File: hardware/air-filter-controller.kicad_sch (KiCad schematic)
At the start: 42 parts, among them J1 TYPE-C-31-M-12, J2 Barrel_Jack, J3 Conn_01x04, J4 Conn_01x03, SW1 SW_Push, SW2 SW_Push, U1 ESP32-S3-WROOM-1-N4, U2 BMP280, U3 MT2492

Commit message: First pass at schematic
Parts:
- removed J3: Conn_01x04, symbol Connector_Generic:Conn_01x04
- added D31, D32, D33, D34: SMAJ5.0A, Diode_SMD:D_SMA, symbol Device:D
- added J13, J14: Conn_01x02, symbol Connector_Generic:Conn_01x02
- added Q1: AO3400A, Package_TO_SOT_SMD:SOT-23, symbol Transistor_FET:AO3400A
- added R11: 100, Resistor_SMD:R_0402_1005Metric, symbol Device:R
- added R39, R40, R44, R45: 1k, Resistor_SMD:R_0402_1005Metric, symbol Device:R
- added R41: 680k, Resistor_SMD:R_0402_1005Metric, symbol Device:R
- added R42: 220k, Resistor_SMD:R_0402_1005Metric, symbol Device:R
- added R43: 10k, Resistor_SMD:R_0402_1005Metric, symbol Device:R
- added SW3, SW4: SW_Push, symbol Switch:SW_Push
- D1: LCSC (none) -> C22452; MPN (none) -> SS54
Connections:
- net USB_D+ is gone; now on net USB_DN: U1.14 (IO20)
- net USB_D- is gone; now on net USB_DP: U1.13 (IO19)
- net +12V: now also R41.1
- net CSB: now also U1.9 (IO16)
- net GND: now also D31.2 (A), D32.2 (A), D33.2 (A), D34.2 (A), J13.1 (Pin_1), J14.1 (Pin_1), Q1.2 (S), R42.2, SW3.2, SW4.2
- net SCK: now also U1.21 (IO13)
- net SDI: now also U1.22 (IO14)
- net SDO: now also U1.8 (IO15)
- net 12V_DIVIDED: now reaches U1.10 (IO17)
- net 12V_DIVIDED: now also R43.2
- net SW2: now reaches U1.11 (IO18)
- net SW2: now also D33.1 (K), R44.2
- net TACH4: now reaches U1.12 (IO8)
- net TACH5: now reaches U1.17 (IO9)
- net TACH6: now reaches U1.18 (IO10)
- net TACH7: now reaches U1.19 (IO11)
- net TACH8: now reaches U1.20 (IO12)
- net FAN_EN: now reaches U1.23 (IO21)
- net FAN_EN: now also R11.1
- net SW3: now reaches U1.31 (IO38)
- net SW3: now also D34.1 (K), R45.2
- net SW1: now reaches U1.38 (IO2)
- net SW1: now also D32.1 (K), R40.2
- net SW0: now reaches U1.39 (IO1)
- net SW0: now also D31.1 (K), R39.2
- net TACH0: now reaches U1.4 (IO4)
- net TACH1: now reaches U1.5 (IO5)
- net TACH2: now reaches U1.6 (IO6)
- net TACH3: now reaches U1.7 (IO7)
- new net: R41.2, R42.1, R43.1
- new net: Q1.1 (G), R11.2
- new net: J14.2 (Pin_2), R45.1
- new net: R40.1, SW4.1
- new net: J13.2 (Pin_2), R44.1
- new net: R39.1, SW3.1
- new net FAN_GND: Q1.3 (D)
- no-connect marks 4 -> 15
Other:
- added sheet fan-output (fan-output.kicad_sch)
- added sheet fan-output1 (fan-output.kicad_sch)
- added sheet fan-output2 (fan-output.kicad_sch)
- added sheet fan-output3 (fan-output.kicad_sch)
- added sheet fan-output4 (fan-output.kicad_sch)
- added sheet fan-output5 (fan-output.kicad_sch)
- added sheet fan-output6 (fan-output.kicad_sch)
- added sheet fan-output7 (fan-output.kicad_sch)
- added sheet fan-output8 (fan-output.kicad_sch)
- note added: "5A crowbar diode"
- note added: "Fan ports"
- note removed: "Crowbar diode"
- moved on the sheet: D3, J1, R10, R7

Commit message: Add buzzer
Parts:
- added BUZZER1: QMB-09B-03, easyeda2kicad:BUZ-TH_BD9.0-P4.00-D0.6-FD, symbol Homebrew:QMB-09B-03
- added R46: 47, Resistor_SMD:R_0603_1608Metric_Pad0.98x0.95mm_HandSolder, symbol Device:R
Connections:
- net GND: now also BUZZER1.2
- net BUZZER: now reaches U1.24 (IO47)
- net BUZZER: now also R46.2
- new net: BUZZER1.1, R46.1
- no-connect marks 15 -> 14
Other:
- moved on the sheet: C10, C11, C12, C13, C8, C9, L1, R6, R8, R9, U3

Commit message: Start placement and routing
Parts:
- removed J2: Barrel_Jack, symbol Connector:Barrel_Jack
- added D35, D36: SMAJ5.0A, Diode_SMD:D_SMA, symbol Device:D
- added DC1: DC-005-2.5A-2.0, Homebrew:CONN-TH_DC-005-2.5A-2.0, symbol Homebrew:DC-005-2.5A-2.0
- added R47: 1k, Resistor_SMD:R_0402_1005Metric, symbol Device:R
- BUZZER1: footprint easyeda2kicad:BUZ-TH_BD9.0-P4.00-D0.6-FD -> Homebrew:BUZ-TH_BD9.0-P4.00-D0.6-FD; LCSC (none) -> C96256; LCSC Part C96256 -> (none)
- D1: footprint (none) -> Diode_SMD:D_SMA
- H1, H2, H3, H4: footprint (none) -> MountingHole:MountingHole_3.2mm_M3_ISO7380; now not fitted
- J1: footprint homebrew:HRO_TYPE-C-31-M-12 -> Homebrew:HRO_TYPE-C-31-M-12
- J13, J14: footprint (none) -> Connector_PinHeader_2.54mm:PinHeader_1x02_P2.54mm_Vertical; now not fitted
- J4: footprint (none) -> Connector_PinHeader_2.54mm:PinHeader_1x03_P2.54mm_Vertical; LCSC (none) -> C6332196
- LED1: footprint easyeda2kicad:LED-ARRAY-SMD_6P-L5.4-W5.0-TL-FD -> Homebrew:LED-ARRAY-SMD_6P-L5.4-W5.0-TL-FD; LCSC (none) -> C219409; LCSC Part C219409 -> (none)
- Q1: LCSC (none) -> C20917
- SW1, SW2, SW3, SW4: footprint (none) -> Homebrew:SW_TACTILE_5.1MM_TS-1187A-C-D-B; LCSC (none) -> C318884
- U2: LCSC (none) -> C83291
- U3: footprint easyeda2kicad:SOT-23-6_L2.9-W1.6-P0.95-LS2.8-BL -> Homebrew:SOT-23-6_L2.9-W1.6-P0.95-LS2.8-BL; LCSC (none) -> C89358; LCSC Part C89358 -> (none)
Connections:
- net 12V_RAW: now also DC1.1
- net BOOT: now also D35.1 (K)
- net EN: now also D36.1 (K), R47.2; no longer SW1.1
- net GND: now also DC1.2
- new net: R47.1, SW1.1
- no-connect marks 14 -> 15
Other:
- note added: "5.5mm/2.1mm Center positive"
- note removed: "Center positive"
- moved on the sheet: R2, SW1, SW2

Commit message: Routing and placement done
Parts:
- added J2: Conn_01x05, Connector_PinHeader_2.54mm:PinHeader_1x05_P2.54mm_Vertical, symbol Connector_Generic:Conn_01x05
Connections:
- net +12V: now also J2.5 (Pin_5)
- net +3V3: now also J2.4 (Pin_4)
- net GND: now also D35.2 (A), D36.2 (A), J2.1 (Pin_1)
- net PWM0: now also U1.25 (IO48)
- net PWM1: now also U1.32 (IO39)
- net SDI: now also U1.8 (IO15); no longer U1.22 (IO14)
- net SDO: now also U1.22 (IO14); no longer U1.8 (IO15)
- net RXD0: now reaches U1.36 (RXD0)
- net RXD0: now also J2.2 (Pin_2)
- net TXD0: now reaches U1.37 (TXD0)
- net TXD0: now also J2.3 (Pin_3)
- no-connect marks 15 -> 11

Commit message: Hardware v1.0
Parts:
- C8: value 47uF -> 22uF 25V; LCSC C96123 -> C12891
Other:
- moved on the sheet: C10, C11, C12, C13, C9, L1, R6, R8, R9, U3

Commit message: Update schematic for v1.1
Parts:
- removed D35: SMAJ5.0A, Diode_SMD:D_SMA, symbol Device:D
- removed J4: Conn_01x03, Connector_PinHeader_2.54mm:PinHeader_1x03_P2.54mm_Vertical, symbol Connector_Generic:Conn_01x03
- removed LED1: HL-AF-5060H271BU46FU79GC-S1-THL, Homebrew:LED-ARRAY-SMD_6P-L5.4-W5.0-TL-FD, symbol Homebrew:HL-AF-5060H271BU46FU79GC-S1-THL
- removed R4, R5: 10, Resistor_SMD:R_0603_1608Metric_Pad0.98x0.95mm_HandSolder, symbol Device:R
- removed R46: 47, Resistor_SMD:R_0603_1608Metric_Pad0.98x0.95mm_HandSolder, symbol Device:R
- removed U2: BMP280, Package_LGA:Bosch_LGA-8_2x2.5mm_P0.65mm_ClockwisePinNumbering, symbol Sensor_Pressure:BMP280
- added C14, C16, C18: 100nF, Capacitor_SMD:C_0402_1005Metric, symbol Device:C
- added C15, C17: 47uF, Capacitor_SMD:C_1206_3216Metric, symbol Device:C
- added D35, D37, D38, D39: WS2812B, Homebrew:LED-SMD_4P-L1.6-W1.5_XL-1615RGBC-WS2812B, symbol LED:WS2812B
- added D40, D41: SMAJ5.0A, Diode_SMD:D_SMA, symbol Device:D
- added D42: D, Diode_SMD:D_SMA, symbol Device:D
- added J15: Conn_01x03, symbol Connector_Generic:Conn_01x03
- added U2: ADP2100, symbol Homebrew:ADP2100
- added U4: AMS1117-3.3, Package_TO_SOT_SMD:SOT-223-3_TabPin2, symbol Regulator_Linear:AMS1117-3.3
- J2: symbol Connector_Generic:Conn_01x05 -> Connector_Generic:Conn_01x06
- L1: value 27uH -> 100uH; LCSC C334252 -> C334254; MPN SWPA8065S220MT -> SWPA8065S101MT
- R3: value 10 -> 220; LCSC C22859 -> C22962
- R8: value 22k 1% -> 15k 1%; LCSC C25768 -> C25756
- R9: value 100k 1% -> 110k 1%; LCSC C25741 -> C25745
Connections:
- net +12V: now also J2.6 (Pin_6); no longer J2.5 (Pin_5)
- net +3V3: now also C17.1, C18.1, U2.1 (VDD), U4.2 (VO); no longer C10.2, C11.1, C12.1, C7.2, L1.2, R9.1
- net 12V_DIVIDED: now also U1.39 (IO1); no longer U1.10 (IO17)
- net 12V_RAW: now also F1.1, D42.1 (K)
- net BUZZER: now also BUZZER1.1
- net GND: now also C7.2, C14.2, C15.2, C16.2, C17.2, C18.2, D35.3 (VSS), D37.3 (VSS), D38.3 (VSS), D39.3 (VSS), D40.2 (A), D41.2 (A), J15.1 (Pin_1), U2.3 (GND), U4.1 (GND); no longer C7.1
- net SW0: now also U1.26 (IO45); no longer U1.39 (IO1)
- net USB_DN: now also U1.13 (IO19); no longer U1.14 (IO20)
- net USB_DP: now also U1.14 (IO20); no longer U1.13 (IO19)
- net VBUS_RAW: now also D42.2 (A)
- net LED_OUT: now reaches R3.2
- net LED_OUT: now also D40.1 (K), J15.2 (Pin_2)
- net LED_B renamed SCL
- net SCL: now also U2.4 (SCL)
- net LED_G: no longer names the net of R3.1
- net LED_G: now also D39.2 (DOUT); no longer U1.33 (IO40)
- net LED_R renamed SDA
- net SDA: now also U2.2 (SDA)
- new net: D38.2 (DOUT), D39.4 (DIN)
- new net: D37.2 (DOUT), D38.4 (DIN)
- new net: D35.2 (DOUT), D37.4 (DIN)
- new net: C7.1, U4.3 (VI)
- new net +5V: C10.2, C11.1, C12.1, C14.1, C15.1, C16.1, D35.1 (VDD), D37.1 (VDD), D38.1 (VDD), D39.1 (VDD), D41.1 (K), J15.3 (Pin_3), J2.5 (Pin_5), L1.2, R9.1
- new net LED_SIGNAL: D35.4 (DIN), U1.33 (IO40)
- new net TACH9: U1.10 (IO17)
- no-connect marks 11 -> 10
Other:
- added sheet fan-output9 (fan-output.kicad_sch)
- note added: "12V -> 5V switching regulator"
- note added: "12V/2A Fuse"
- note added: "5V -> 3.3V linear regulator"
- note added: "Buttons"
- note added: "Differential pressure sensor"
- note added: "Indicator LEDs"
- note added: "Power input"
- note removed: "12/2A Fuse"
- note removed: "3.3V switching regulator"
- note removed: "ESP32-S3 has drive strength settings on IO pins. Small resistors as a safety measure."
- note removed: "Power selection via jumper. "12V" will actually be 5V when connected to USB. That's enough to program the MCU, but not run the fans."
- note removed: "Pressure sensor"
- moved on the sheet: C5, D1, D2, DC1, F1, H1, H2, H3, H4, Q1, R11, R41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

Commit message: More schematic updates for v1.1
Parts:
- added U5: ZX-SH1.0-4PWT, easyeda2kicad:CONN-SMD_4P-P1.00_MEGASTAR_ZX-SH1.0-4PWT, symbol Homebrew:ZX-SH1.0-4PWT
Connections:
- net SCK is gone; now on net TACH9: U1.21 (IO13)
- net +3V3: now also U5.2
- net +5V: now also C7.1, U4.3 (VI)
- net GND: now also U5.1
- net SCL: now also U5.4
- net SDA: now also U5.3
- net TACH9: no longer U1.10 (IO17)
- net CSB: no longer names the net of U1.9 (IO16)
- net SDI: no longer names the net of U1.8 (IO15)
- net SDO: no longer names the net of U1.22 (IO14)
- no-connect marks 10 -> 16

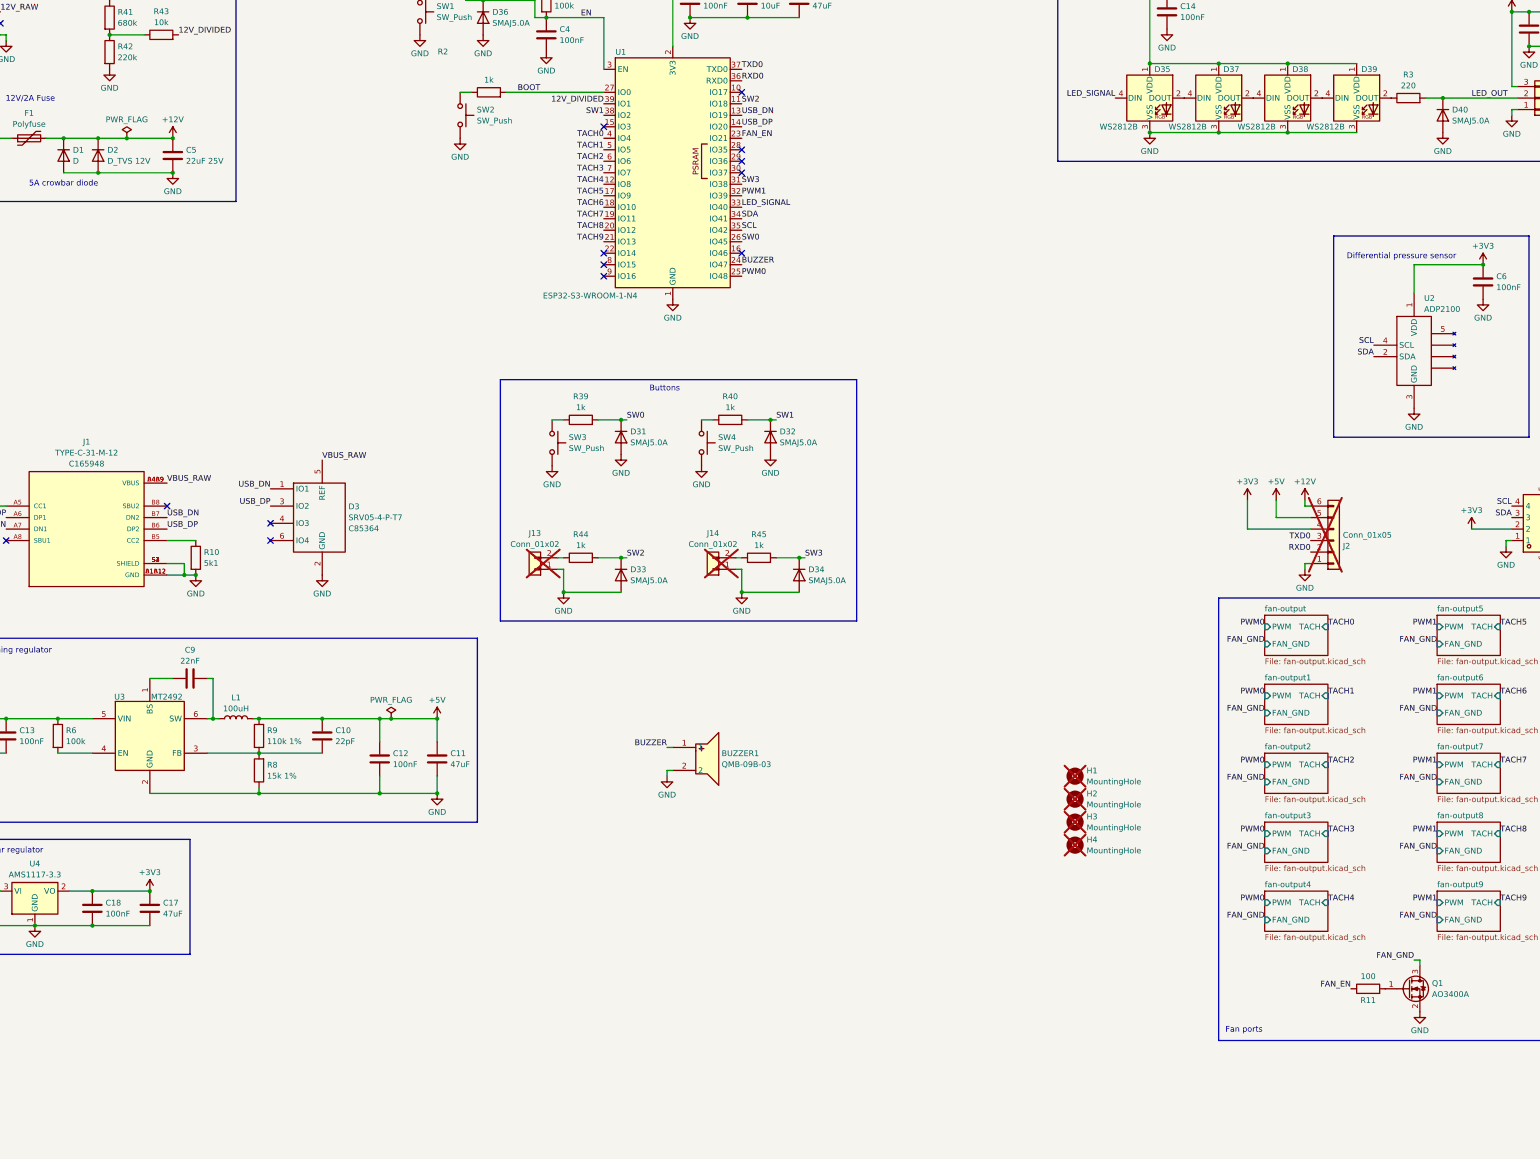
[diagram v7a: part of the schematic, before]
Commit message: More schematic updates for v1.1:
- Add connectors for offboard PMS5003 sensors
- Add ADP2100 differential pressure sensor
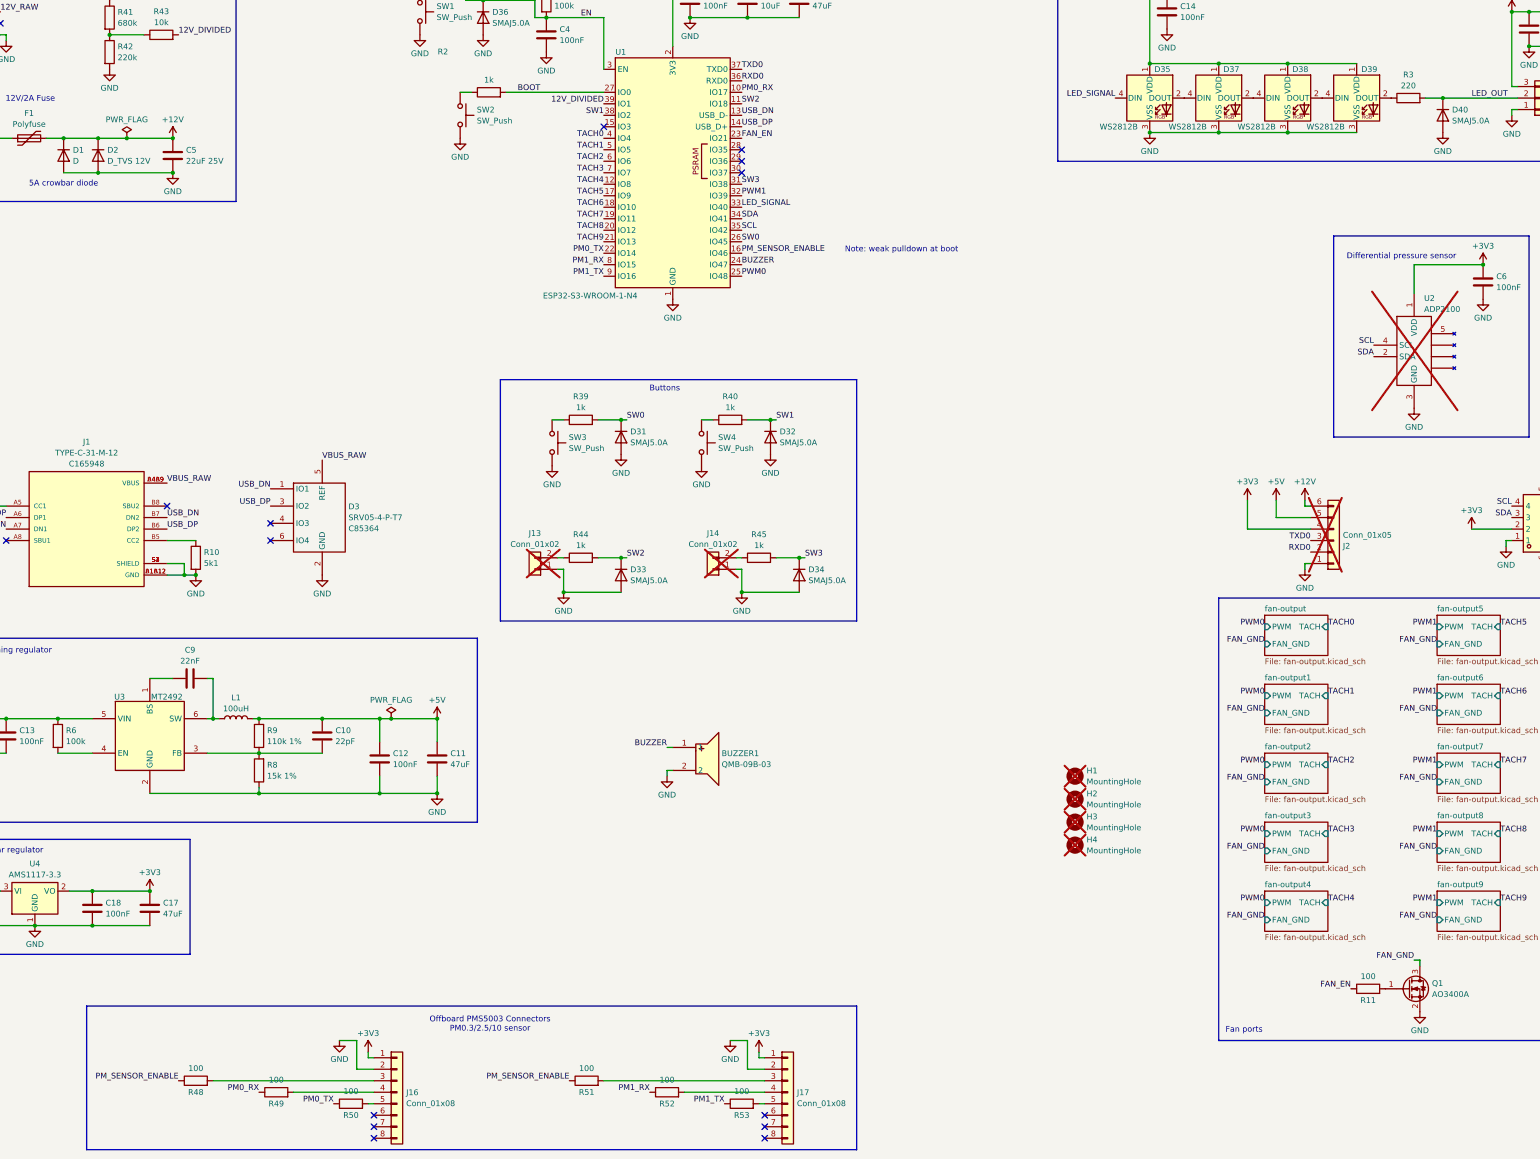
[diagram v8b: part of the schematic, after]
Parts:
- added J16, J17: Conn_01x08, easyeda2kicad:CONN-TH_8P-P1.25_HCTL_HC-1.25-8A, symbol Connector_Generic:Conn_01x08
- added R48, R49, R50, R51, R52, R53: 100, Resistor_SMD:R_0603_1608Metric_Pad0.98x0.95mm_HandSolder, symbol Device:R
- J15: footprint (none) -> Connector_PinHeader_2.54mm:PinHeader_1x03_P2.54mm_Vertical
- U2: footprint (none) -> Homebrew:ADP2100_HandSoldering; now not fitted
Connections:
- net +3V3: now also J16.1 (Pin_1), J17.1 (Pin_1)
- net GND: now also J16.2 (Pin_2), J17.2 (Pin_2)
- net PM0_RX: now reaches U1.10 (IO17)
- net PM0_RX: now also R49.1
- net PM_SENSOR_ENABLE: now reaches U1.16 (IO46)
- net PM_SENSOR_ENABLE: now also R48.1, R51.1
- net PM0_TX: now reaches U1.22 (IO14)
- net PM0_TX: now also R50.1
- net PM1_RX: now reaches U1.8 (IO15)
- net PM1_RX: now also R52.1
- net PM1_TX: now reaches U1.9 (IO16)
- net PM1_TX: now also R53.1
- new net: J17.5 (Pin_5), R53.2
- new net: J17.3 (Pin_3), R51.2
- new net: J17.4 (Pin_4), R52.2
- new net: J16.5 (Pin_5), R50.2
- new net: J16.3 (Pin_3), R48.2
- new net: J16.4 (Pin_4), R49.2
- no-connect marks 16 -> 17
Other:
- note added: "Note: weak pulldown at boot"
- note added: "Offboard PMS5003 Connectors PM0.3/2.5/10 sensor"
